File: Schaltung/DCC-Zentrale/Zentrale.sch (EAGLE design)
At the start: 6 parts, among them IC1 ATMEGA644-20PU, IC2 L6203, IC3 MAX232, IC4 FT232BL, Q1 18,432 MHz

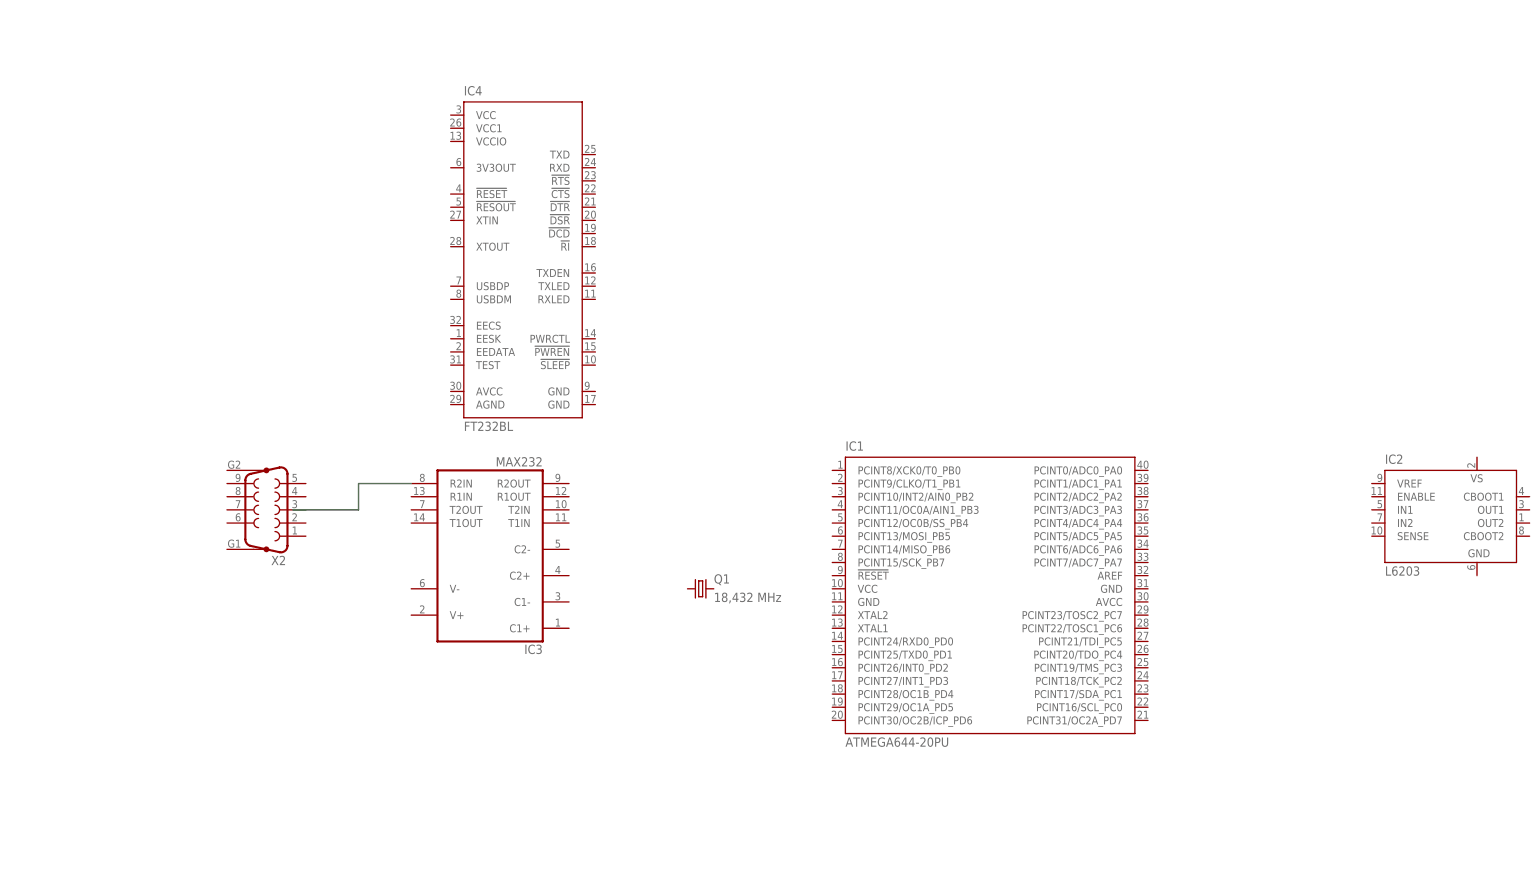
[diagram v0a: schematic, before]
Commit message: Added L6203 to schematic
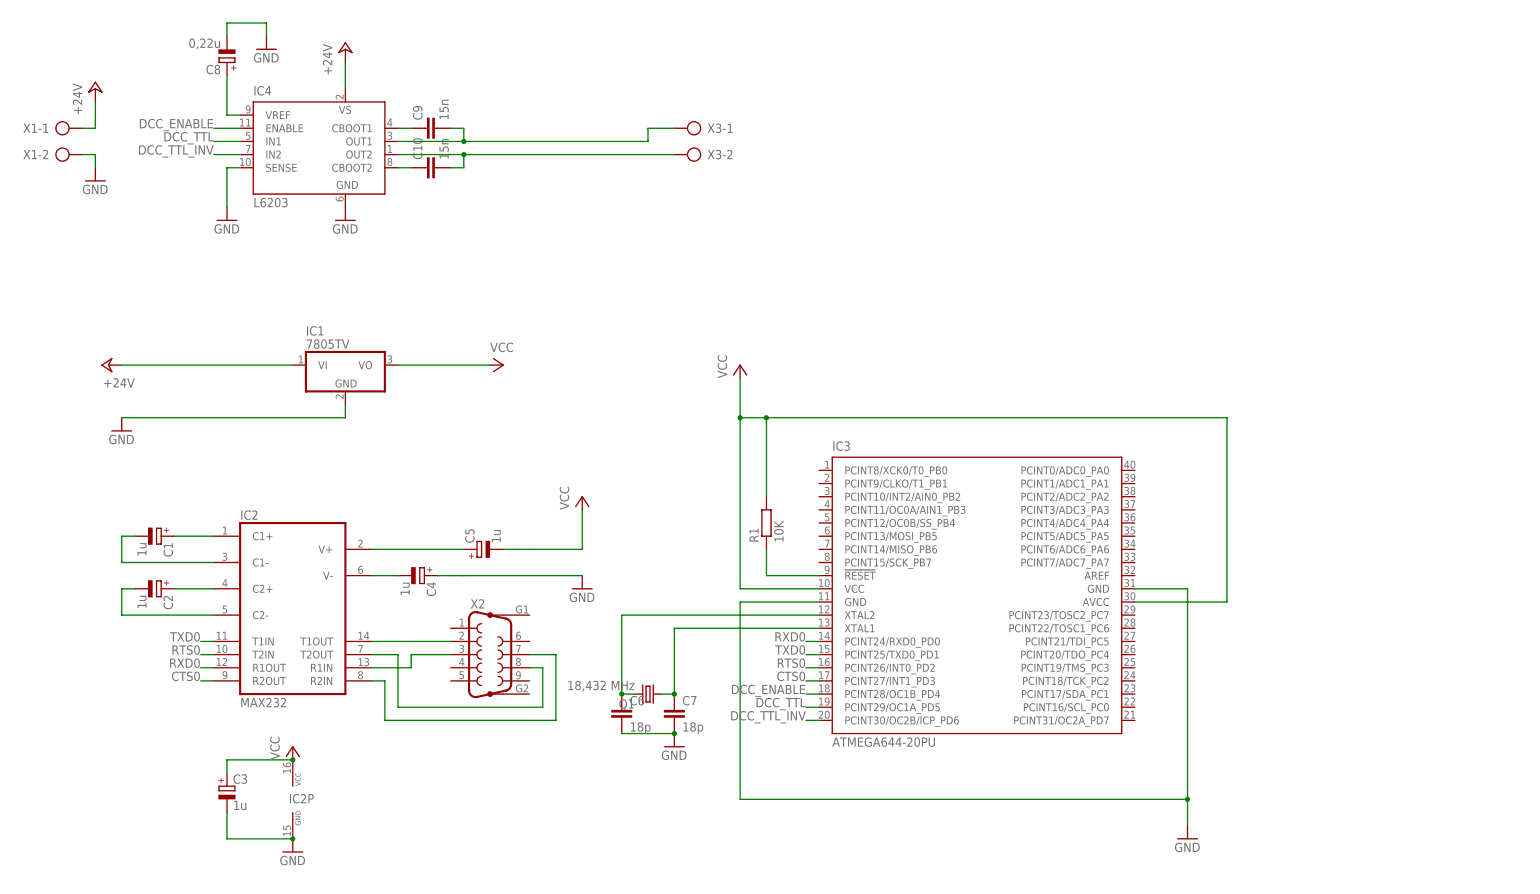
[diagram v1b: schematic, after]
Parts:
- added C1, C2, C3, C4, C5: 1u, resistor:CPOL-EUTT2D5
- added C10, C9: 15n, resistor:C-EU025-025X050
- added C6, C7: 18p, resistor:C-EU025-025X050
- added C8: 0,22u, resistor:CPOL-EUTT2D5
- added R1: 10K, resistor:R-EU_0204/5
- added X1, X3: (no value), con-ptr500:AK500/2
- IC1: value ATMEGA644-20PU -> 7805TV; device atmel:ATMEGA644-20PU -> linear:7805TV
- IC2: value L6203 -> MAX232; device st-microelectronics:L6203 -> maxim:MAX232
- IC3: value MAX232 -> ATMEGA644-20PU; device maxim:MAX232 -> atmel:ATMEGA644-20PU
- IC4: value FT232BL -> L6203; device ftdichip:FT232BL -> st-microelectronics:L6203
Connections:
- new net +24V: IC1.VI, IC4.VS, X1-1.KL
- new net CTS0: IC2G$1.R2OUT, IC3.PCINT27/INT1_PD3
- new net DCC_ENABLE: IC3.PCINT28/OC1B_PD4, IC4.ENABLE
- new net DCC_TTL: IC3.PCINT29/OC1A_PD5, IC4.IN1
- new net DCC_TTL_INV: IC3.PCINT30/OC2B/ICP_PD6, IC4.IN2
- new net GND: C3.-, C4.+, C6.2, C7.2, C8.-, IC1.GND, IC2P.GND, IC3.GND, IC3.GND@1, IC4.GND, IC4.SENSE, X1-2.KL
- new net N$10: C2.+, IC2G$1.C2+
- new net N$11: C2.-, IC2G$1.C2-
- new net N$12: C4.-, IC2G$1.V-
- new net N$13: C5.+, IC2G$1.V+
- new net N$14: IC3.!RESET, R1.1
- new net N$15: C6.1, IC3.XTAL2, Q1.2
- new net N$16: C7.1, IC3.XTAL1, Q1.1
- new net N$17: C9.2, IC4.OUT1, X3-1.KL
- new net N$18: C10.2, IC4.OUT2, X3-2.KL
- new net N$19: C10.1, IC4.CBOOT2
- new net N$2: IC2G$1.R2IN, X2.7
- new net N$21: C9.1, IC4.CBOOT1
- new net N$3: C8.+, IC4.VREF
- new net N$6: IC2G$1.T1OUT, X2.2
- new net N$7: IC2G$1.R1IN, X2.3
- new net N$8: C1.+, IC2G$1.C1+
- new net N$9: C1.-, IC2G$1.C1-
- new net RTS0: IC2G$1.T2IN, IC3.PCINT26/INT0_PD2
- new net RXD0: IC2G$1.R1OUT, IC3.PCINT24/RXD0_PD0
- new net TXD0: IC2G$1.T1IN, IC3.PCINT25/TXD0_PD1
- new net VCC: C3.+, C5.-, IC1.VO, IC2P.VCC, IC3.AVCC, IC3.VCC, R1.2
- net N$1: now also IC2G$1.T2OUT, X2.8; no longer IC3G$1.R2IN
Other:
- moved on the sheet: Q1, X2

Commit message: Added SENSE and ADC connection
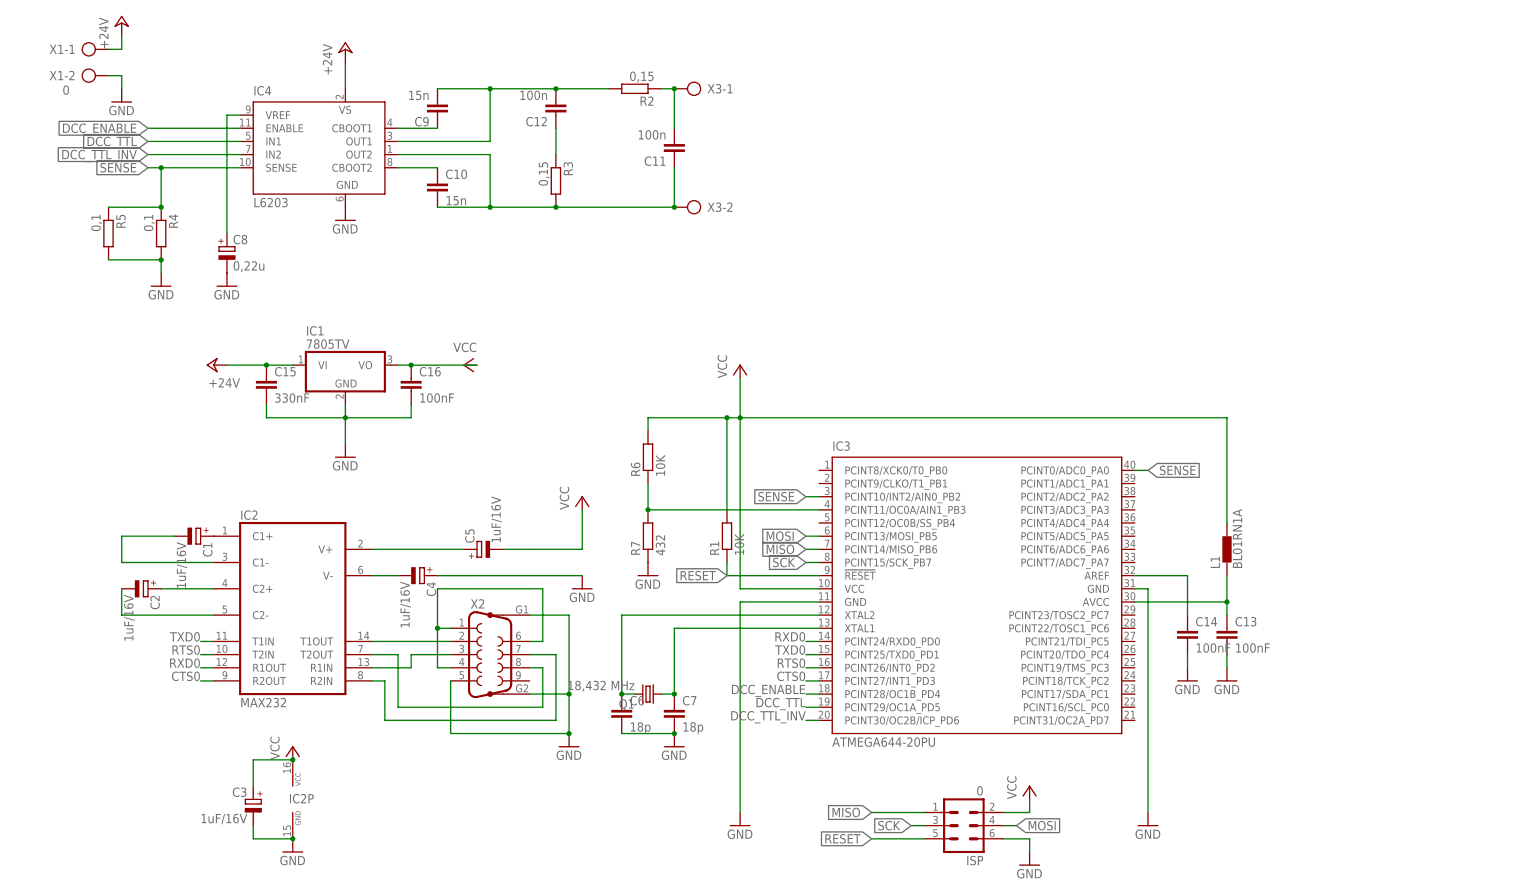
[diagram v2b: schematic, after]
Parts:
- added C11, C12: 100n, resistor:C-EU025-025X050
- added C13, C14, C16: 100nF, resistor:C-EU025-025X050
- added C15: 330nF, resistor:C-EU025-025X050
- added ISP: 0, con-harting-ml:ML6
- added L1: BL01RN1A, inductors:BL01RN1A
- added R2, R3: 0,15, resistor:R-EU_0204/5
- added R4, R5: 0,1, resistor:R-EU_0204/5
- added R6: 10K, resistor:R-EU_0204/5
- added R7: 432, resistor:R-EU_0204/5
- C1, C2, C3, C4, C5: value 1u -> 1uF/16V
- X1: value (none) -> 0
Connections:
- new net MISO: IC3.PCINT14/MISO_PB6, ISP.1
- new net MOSI: IC3.PCINT13/MOSI_PB5, ISP.4
- new net N$20: C13.1, IC3.AVCC, L1.1
- new net N$22: X2.1, X2.4, X2.6
- new net N$23: IC3.PCINT11/OC0A/AIN1_PB3, R6.1, R7.2
- new net N$4: C11.2, R2.1, X3-1.KL
- new net N$5: C12.1, R3.1
- new net RESET: IC3.!RESET, ISP.5, R1.1
- new net SCK: IC3.PCINT15/SCK_PB7, ISP.3
- new net SENSE: IC3.PCINT0/ADC0_PA0, IC3.PCINT10/INT2/AIN0_PB2, IC4.SENSE, R4.1, R5.1
- net +24V: now also C15.1
- net GND: now also C13.2, C14.2, C15.2, C16.2, ISP.6, R4.2, R5.2, R7.1, X2.5, X2.G1, X2.G2; no longer IC4.SENSE
- net N$14: now also C14.1, IC3.AREF; no longer IC3.!RESET, R1.1
- net N$17: now also C12.2, R2.2; no longer X3-1.KL
- net N$18: now also C11.1, R3.2
- net VCC: now also C16.1, ISP.2, L1.2, R6.2; no longer IC3.AVCC
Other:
- moved on the sheet: C1, C10, C2, C3, C8, C9, R1, X1-1, X1-2, X3-1, X3-2
